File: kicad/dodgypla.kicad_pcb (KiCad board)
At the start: 2 copper layers, 20.3 x 38.1 mm, 10 parts, among them J1 PLA_Conn, J2 PAD_TCK, J3 PAD_TMS, J4 PAD_TDO, J5 PAD_TDI, U1 AMS1117, U2 XC9536XL-5VQG44C

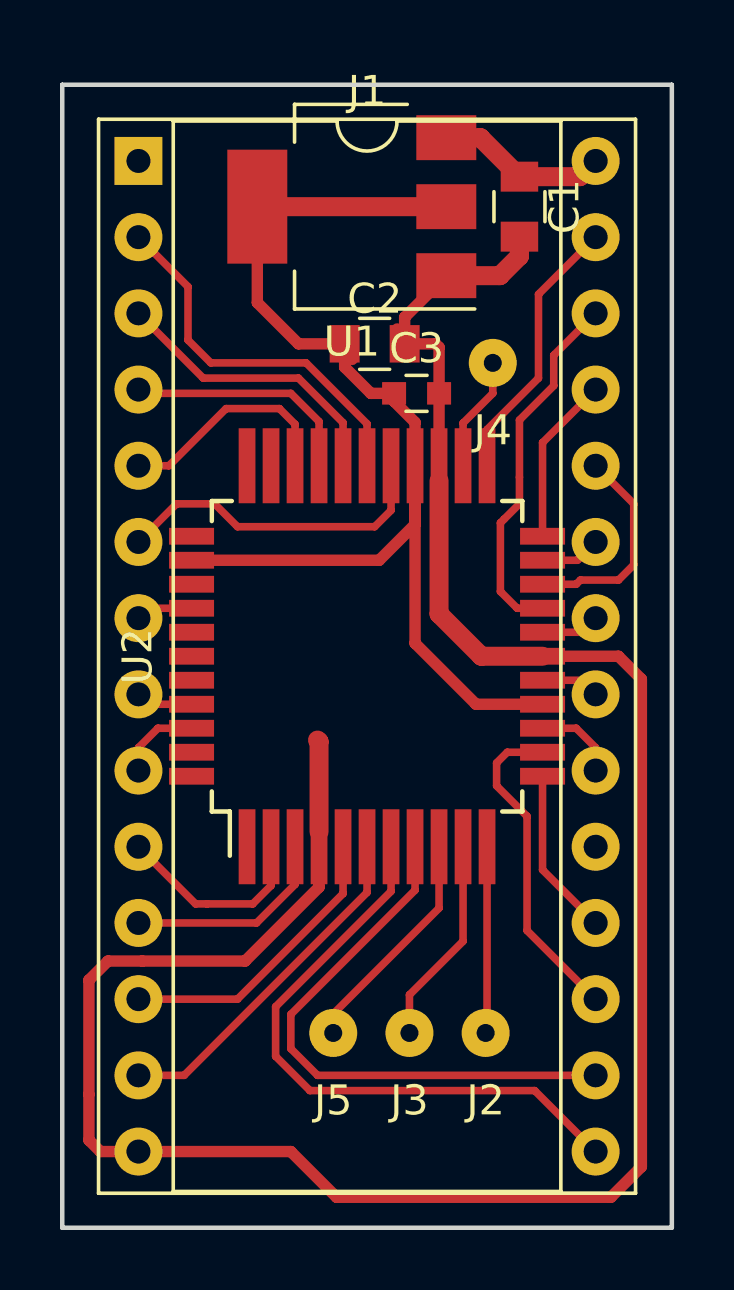
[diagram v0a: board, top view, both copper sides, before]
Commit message: Converting to two-layer board for PCB manufacturing.
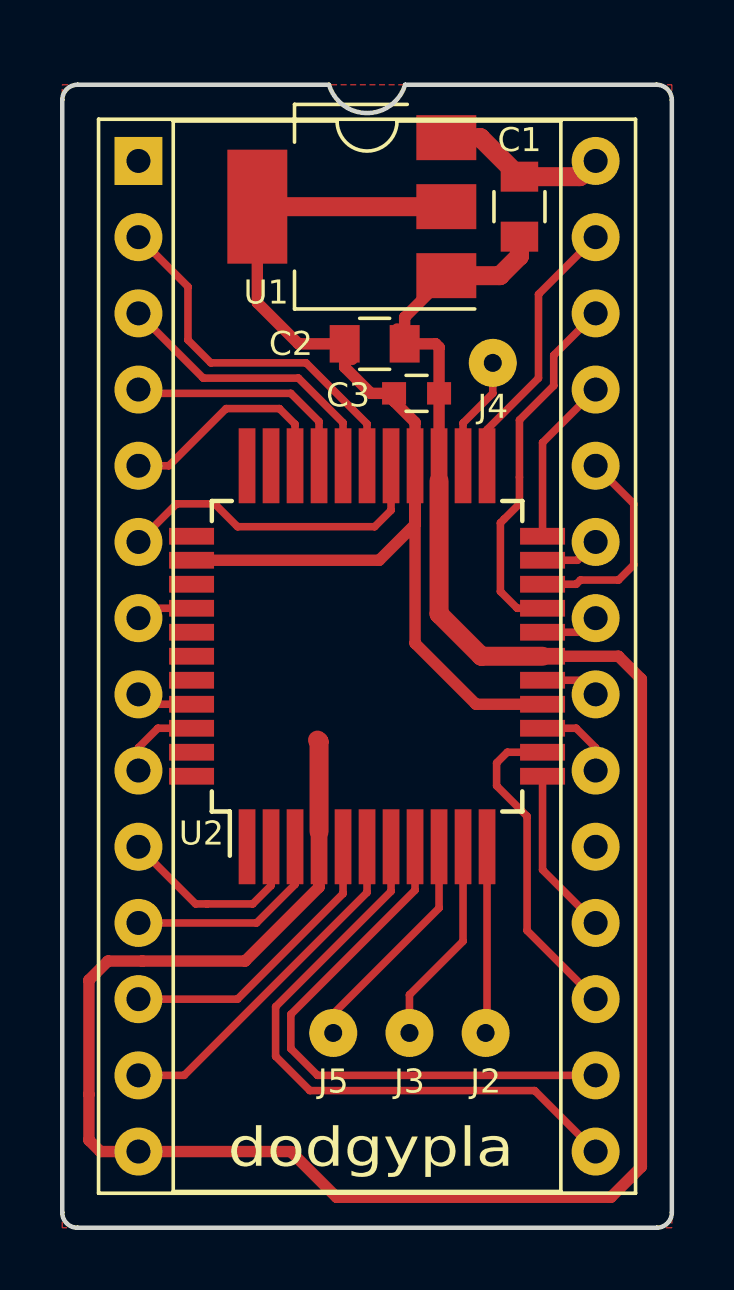
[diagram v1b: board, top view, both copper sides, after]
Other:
- outline, holes or cut-outs redrawn
- board text added: "dodgypla"
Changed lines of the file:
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@@
-(kicad_pcb (version 4) (host pcbnew 4.0.7)
+(kicad_pcb (version 20171130) (host pcbnew "(5.1.0)-1")
   (general
-    (links 43)
-    (no_connects 0)
-    (area 120.889523 74.346 143.270477 117.324)
     (thickness 1.6)
-    (drawings 5)
+    (drawings 12)
     (tracks 186)
     (zones 0)
@@
   )
   (setup
-    (last_trace_width 0.381)
+    (last_trace_width 0.254)
     (user_trace_width 0.381)
     (user_trace_width 0.635)
@@
     (zone_45_only no)
     (trace_min 0.2)
-    (segment_width 0.2)
-    (edge_width 0.15)
     (via_size 0.6)
     (via_drill 0.4)
@@
     (uvia_min_size 0.2)
     (uvia_min_drill 0.1)
+    (edge_width 0.15)
+    (segment_width 0.2)
     (pcb_text_width 0.3)
     (pcb_text_size 1.5 1.5)
@@
     (pad_to_mask_clearance 0.2)
     (aux_axis_origin 0 0)
-    (visible_elements 7FFFF7FF)
+    (visible_elements 7FFFFFFF)
     (pcbplotparams
       (layerselection 0x00000_00000001)
       (usegerberextensions false)
+      (usegerberattributes false)
+      (usegerberadvancedattributes false)
+      (creategerberjobfile false)
       (excludeedgelayer true)
       (linewidth 0.100000)
@@
       (hpglpennumber 1)
       (hpglpenspeed 20)
-      (hpglpendiameter 15)
-      (hpglpenoverlay 2)
+      (hpglpendiameter 15.000000)
       (psnegative false)
       (psa4output false)
@@
       (drillshape 1)
       (scaleselection 1)
-      (outputdirectory out/))
+      (outputdirectory "out/"))
   )
   (net 0 "")
@@
     (descr "28-lead though-hole mounted DIP package, row spacing 15.24 mm (600 mils), Socket")
     (tags "THT DIP DIL PDIP 2.54mm 15.24mm 600mil Socket")
-    (fp_text reference J1 (at 7.62 -2.33) (layer F.SilkS)
+    (fp_text reference J1 (at 0.0635 -1.651) (layer F.SilkS) hide
       (effects (font (size 1 1) (thickness 0.15)))
     )
@@
     (tags "capacitor 0603")
     (attr smd)
-    (fp_text reference C3 (at 0 -1.5) (layer F.SilkS)
-      (effects (font (size 1 1) (thickness 0.15)))
+    (fp_text reference C3 (at -2.286 0.0635) (layer F.SilkS)
+      (effects (font (size 0.8 0.8) (thickness 0.12)))
     )
     (fp_text value 0.1uF (at 0 1.5) (layer F.Fab)
@@
     (descr "solder Pin_ diameter 1.0mm, hole diameter 1.0mm (press fit), length 10.0mm")
     (tags "solder Pin_ press fit")
-    (fp_text reference J2 (at 0 2.25) (layer F.SilkS)
-      (effects (font (size 1 1) (thickness 0.15)))
+    (fp_text reference J2 (at 0 1.615) (layer F.SilkS)
+      (effects (font (size 0.8 0.8) (thickness 0.12)))
     )
     (fp_text value PAD_TCK (at 0 -2.05) (layer F.Fab)
@@
     (descr "solder Pin_ diameter 1.0mm, hole diameter 1.0mm (press fit), length 10.0mm")
     (tags "solder Pin_ press fit")
-    (fp_text reference J3 (at 0 2.25) (layer F.SilkS)
-      (effects (font (size 1 1) (thickness 0.15)))
+    (fp_text reference J3 (at 0 1.615) (layer F.SilkS)
+      (effects (font (size 0.8 0.8) (thickness 0.12)))
     )
     (fp_text value PAD_TMS (at 0 -2.05) (layer F.Fab)
@@
     (descr "solder Pin_ diameter 1.0mm, hole diameter 1.0mm (press fit), length 10.0mm")
     (tags "solder Pin_ press fit")
-    (fp_text reference J4 (at 0 2.25) (layer F.SilkS)
-      (effects (font (size 1 1) (thickness 0.15)))
+    (fp_text reference J4 (at 0 1.4605) (layer F.SilkS)
+      (effects (font (size 0.8 0.8) (thickness 0.12)))
     )
     (fp_text value PAD_TDO (at 0 -2.05) (layer F.Fab)
@@
     (descr "solder Pin_ diameter 1.0mm, hole diameter 1.0mm (press fit), length 10.0mm")
     (tags "solder Pin_ press fit")
-    (fp_text reference J5 (at 0 2.25) (layer F.SilkS)
-      (effects (font (size 1 1) (thickness 0.15)))
+    (fp_text reference J5 (at 0 1.615) (layer F.SilkS)
+      (effects (font (size 0.8 0.8) (thickness 0.12)))
     )
     (fp_text value PAD_TDI (at 0 -2.05) (layer F.Fab)
@@
     (tags "CMS SOT")
     (attr smd)
-    (fp_text reference U1 (at 0 -4.5 180) (layer F.SilkS)
-      (effects (font (size 1 1) (thickness 0.15)))
+    (fp_text reference U1 (at 2.8575 -2.8575 180) (layer F.SilkS)
+      (effects (font (size 0.8 0.8) (thickness 0.12)))
     )
     (fp_text value AMS1117 (at 0 4.5 180) (layer F.Fab)
@@
     (tags "capacitor 0805")
     (attr smd)
-    (fp_text reference C1 (at 0 -1.5 270) (layer F.SilkS)
-      (effects (font (size 1 1) (thickness 0.15)))
+    (fp_text reference C1 (at -2.2225 0) (layer F.SilkS)
+      (effects (font (size 0.8 0.8) (thickness 0.12)))
     )
     (fp_text value 3.3uF (at 0 1.75 270) (layer F.Fab)
@@
     (tags "capacitor 0805")
     (attr smd)
-    (fp_text reference C2 (at 0 -1.5) (layer F.SilkS)
-      (effects (font (size 1 1) (thickness 0.15)))
+    (fp_text reference C2 (at -2.794 0) (layer F.SilkS)
+      (effects (font (size 0.8 0.8) (thickness 0.12)))
     )
     (fp_text value 3.3uF (at 0 1.75) (layer F.Fab)
@@
     (tags "QFP 0.8")
     (attr smd)
-    (fp_text reference U2 (at 0 -7.65 90) (layer F.SilkS)
-      (effects (font (size 1 1) (thickness 0.15)))
+    (fp_text reference U2 (at -5.9055 -5.5245 180) (layer F.SilkS)
+      (effects (font (size 0.8 0.8) (thickness 0.12)))
     )
     (fp_text value XC9536XL-5VQG44C (at 0 7.65 90) (layer F.Fab)
@@
     )
   )
+  (gr_text dodgypla (at 131.572 113.792) (layer F.SilkS)
+    (effects (font (size 1.3 1.5) (thickness 0.3)))
+  )
+  (gr_arc (start 141.097 115.951) (end 141.097 116.459) (angle -90) (layer Edge.Cuts) (width 0.15))
+  (gr_arc (start 121.793 115.951) (end 121.285 115.951) (angle -90) (layer Edge.Cuts) (width 0.15))
+  (gr_arc (start 121.793 78.867) (end 121.793 78.359) (angle -90) (layer Edge.Cuts) (width 0.15))
+  (gr_arc (start 141.097 78.867) (end 141.605 78.867) (angle -90) (layer Edge.Cuts) (width 0.15))
+  (gr_arc (start 131.445 77.978) (end 130.175001 78.358999) (angle -146.6015115) (layer Edge.Cuts) (width 0.15))
+  (gr_line (start 141.097 78.359) (end 132.715 78.359) (layer Edge.Cuts) (width 0.15))
+  (gr_line (start 121.793 78.359) (end 130.175 78.359) (layer Edge.Cuts) (width 0.15))
   (gr_text "NOTE: This board is designed\nfor home etching" (at 132.08 75.946) (layer Cmts.User)
     (effects (font (size 1 1) (thickness 0.15)))
   )
-  (gr_line (start 121.285 116.459) (end 121.285 78.359) (angle 90) (layer Edge.Cuts) (width 0.15))
-  (gr_line (start 141.605 116.459) (end 121.285 116.459) (angle 90) (layer Edge.Cuts) (width 0.15))
-  (gr_line (start 141.605 78.359) (end 141.605 116.459) (angle 90) (layer Edge.Cuts) (width 0.15))
-  (gr_line (start 121.285 78.359) (end 141.605 78.359) (angle 90) (layer Edge.Cuts) (width 0.15))
+  (gr_line (start 121.285 115.951) (end 121.285 78.867) (angle 90) (layer Edge.Cuts) (width 0.15))
+  (gr_line (start 141.097 116.459) (end 121.793 116.459) (angle 90) (layer Edge.Cuts) (width 0.15))
+  (gr_line (start 141.605 78.867) (end 141.605 115.951) (angle 90) (layer Edge.Cuts) (width 0.15))
   (segment (start 136.525 81.423) (end 138.541 81.423) (width 0.635) (layer F.Cu) (net 1))
   (segment (start 138.541 81.423) (end 139.065 80.899) (width 0.635) (layer F.Cu) (net 1))

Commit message: Converting to two-layer board for PCB manufacturing.
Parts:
- U2: value XC9536XL-5VQG44C -> XC9536XL-10VQ44C
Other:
- board text removed: "NOTE: This board is designed for home etching"
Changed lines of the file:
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@@
   (general
     (thickness 1.6)
-    (drawings 12)
+    (drawings 11)
     (tracks 186)
     (zones 0)
@@
       (effects (font (size 0.8 0.8) (thickness 0.12)))
     )
-    (fp_text value XC9536XL-5VQG44C (at 0 7.65 90) (layer F.Fab)
+    (fp_text value XC9536XL-10VQ44C (at 0 7.65 90) (layer F.Fab)
       (effects (font (size 1 1) (thickness 0.15)))
     )
@@
   (gr_line (start 141.097 78.359) (end 132.715 78.359) (layer Edge.Cuts) (width 0.15))
   (gr_line (start 121.793 78.359) (end 130.175 78.359) (layer Edge.Cuts) (width 0.15))
-  (gr_text "NOTE: This board is designed\nfor home etching" (at 132.08 75.946) (layer Cmts.User)
-    (effects (font (size 1 1) (thickness 0.15)))
-  )
   (gr_line (start 121.285 115.951) (end 121.285 78.867) (angle 90) (layer Edge.Cuts) (width 0.15))
   (gr_line (start 141.097 116.459) (end 121.793 116.459) (angle 90) (layer Edge.Cuts) (width 0.15))

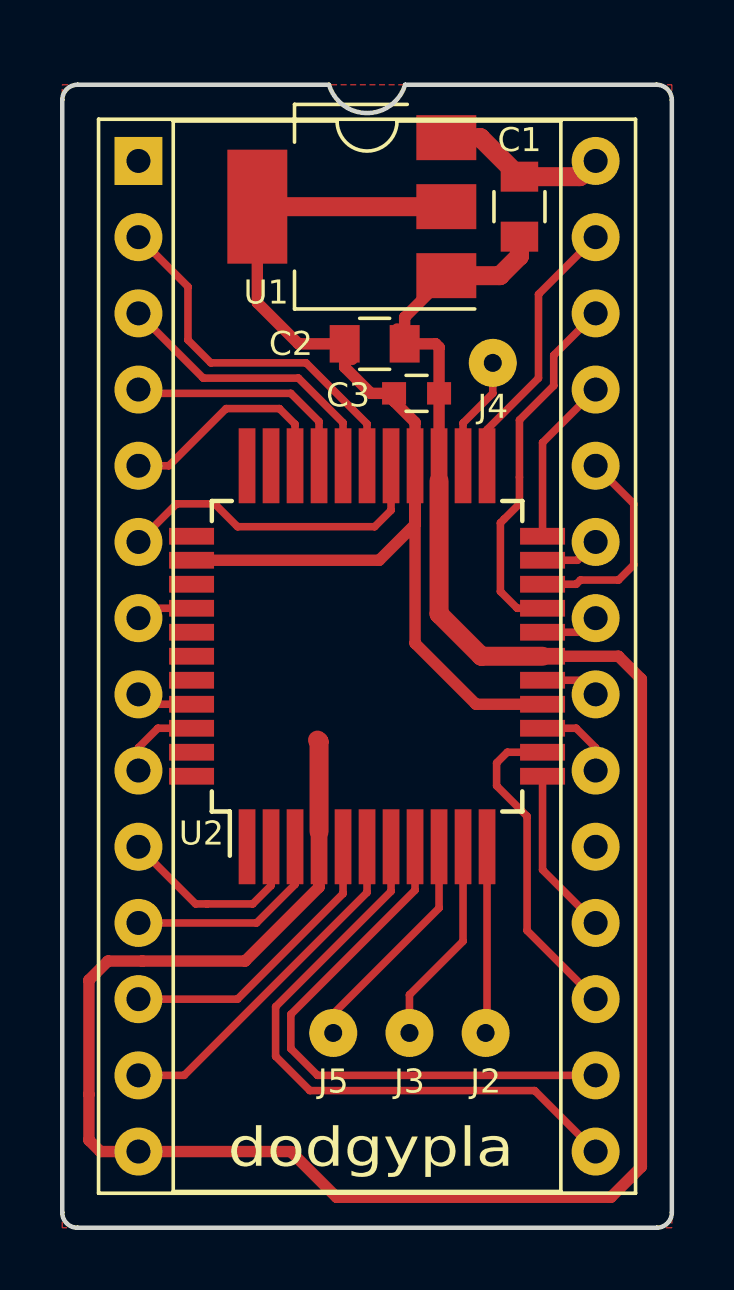
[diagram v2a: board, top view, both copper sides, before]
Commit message: Converting to two-layer board for PCB manufacturing.
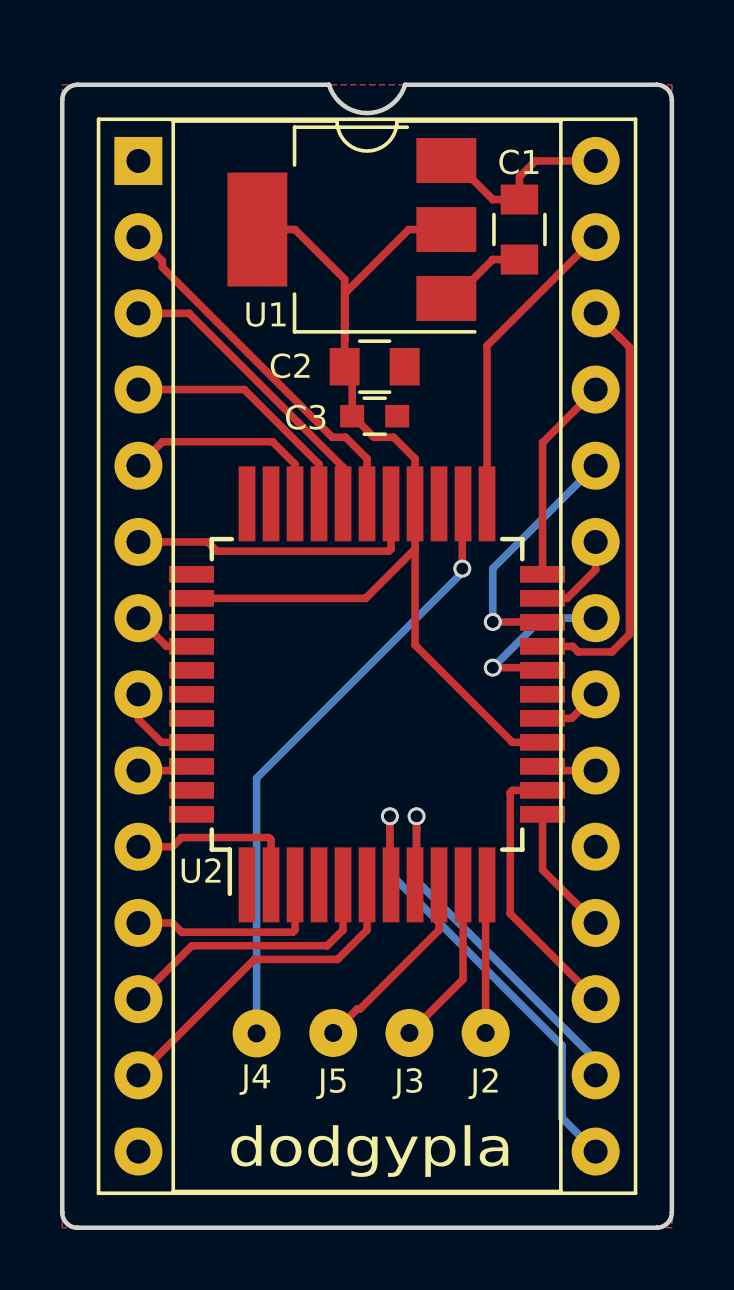
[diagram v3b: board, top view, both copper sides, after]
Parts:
- moved J4 23.7 mm to (127.8, 110.0)
- moved C3 1.59 mm to (131.7, 89.4)
- moved U2 1.27 mm to (131.4, 98.7)
- moved C1 0.76 mm to (136.5, 83.2)
- moved C2 0.76 mm to (131.7, 87.8)
- moved U1 0.76 mm to (130.9, 83.2)
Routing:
- net GND: track 80.9 -> 2.98 mm
- net /JTAG_TDO: track 3.84 -> 20.5 mm, vias 0 -> 1
- net /PLA_KERNAL: track 19.5 -> 13.4 mm, vias 0 -> 1
- net /PLA_CHAROM: track 20.8 -> 16.3 mm, vias 0 -> 1
- net /PLA_GAME: track 1.96 -> 5.81 mm, vias 0 -> 1
- net +3V3: track 40.0 -> 36.7 mm
- net /JTAG_TMS: track 8.57 -> 5.68 mm
- net /JTAG_TDI: track 9.32 -> 6.45 mm
- net /PLA_BA: track 12.2 -> 14.4 mm
- net /PLA_ROMH: track 7.92 -> 6.08 mm
- net /JTAG_TCK: track 6.73 -> 4.96 mm
- net /PLA_BASIC: track 10.9 -> 9.17 mm
- net /PLA_VA14: track 8.73 -> 7.18 mm
- net /PLA_A13: track 13.6 -> 12.3 mm
- net /PLA_A14: track 11.4 -> 10.2 mm
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- added copper zone on B.Cu, net GND

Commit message: Converting to two-layer board for PCB manufacturing.
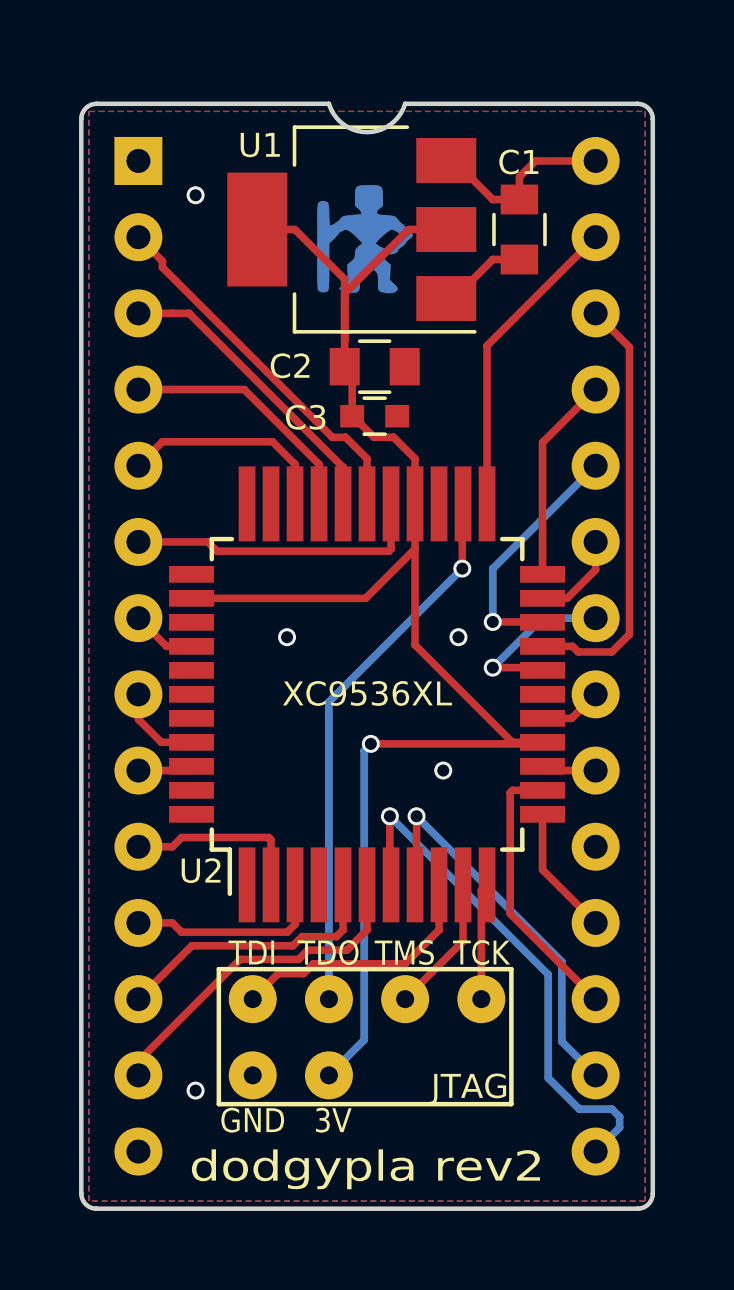
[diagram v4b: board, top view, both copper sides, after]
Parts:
- removed J3: PAD_TMS, desaster_footprints:testpad_1.6mm
- removed J4: PAD_TDO, desaster_footprints:testpad_1.6mm
- removed J5: PAD_TDI, desaster_footprints:testpad_1.6mm
- added G***: LOGO, Logo:bigby2, B.Cu at (131.3, 83.4)
- J2: value PAD_TCK -> JTAG; footprint desaster_footprints:testpad_1.6mm -> Pin_Headers:Pin_Header_Straight_2x04_Pitch2.54mm
- U1: footprint TO_SOT_Packages_SMD:SOT-223-3Lead_TabPin2 -> TO_SOT_Packages_SMD:SOT-223-3_TabPin2
- U2: value XC9536XL-10VQ44C -> XC9536XL
- moved J2 1.14 mm to (135.3, 108.8), turned to 270 degrees
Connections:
- J1 pad 1: /PLA_FE -> (no net)
- J1 pad 19: /PLA_OE -> (no net)
- U2 pad 1: Net-(U2-Pad1) -> (no net)
- U2 pad 32: Net-(U2-Pad32) -> (no net)
- U2 pad 33: Net-(U2-Pad33) -> (no net)
- U2 pad 34: Net-(U2-Pad34) -> (no net)
- U2 pad 36: Net-(U2-Pad36) -> (no net)
- U2 pad 38: Net-(U2-Pad38) -> (no net)
- U2 pad 39: Net-(U2-Pad39) -> (no net)
- U2 pad 40: Net-(U2-Pad40) -> (no net)
- U2 pad 43: Net-(U2-Pad43) -> (no net)
- U2 pad 44: Net-(U2-Pad44) -> (no net)
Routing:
- net +3V3: track 36.7 -> 54.1 mm, vias 0 -> 1
- net /JTAG_TDI: track 6.45 -> 8.67 mm
- net /JTAG_TDO: track 20.5 -> 18.5 mm
- net /PLA_CHAROM: track 16.3 -> 17.6 mm
- net /JTAG_TCK: track 4.96 -> 3.89 mm
- net /JTAG_TMS: track 5.68 -> 4.61 mm
- net GND: vias 0 -> 5
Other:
- board size 20.3 x 38.1 mm -> 19 x 36.8 mm
- board text added: "3V"
- board text added: "GND"
- board text added: "TCK"
- board text added: "TDI"
- board text added: "TDO"
- board text added: "TMS"
- board text added: "dodgypla rev2"
- board text added: "github.com/hackup/c64-dodgypla credits: desaster, nightfall"
- board text removed: "dodgypla"
